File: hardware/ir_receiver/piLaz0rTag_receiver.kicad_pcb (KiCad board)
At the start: 2 copper layers, 47 x 43.2 mm, 5 parts

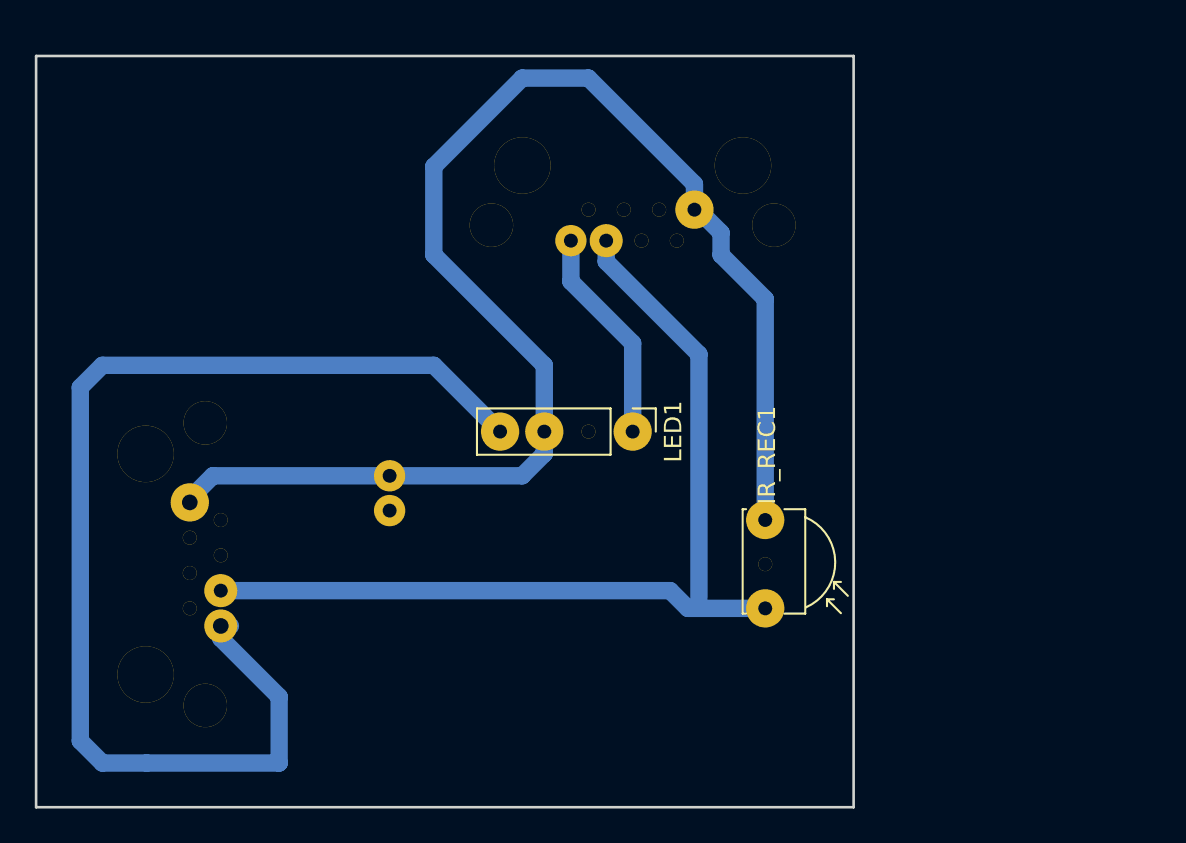
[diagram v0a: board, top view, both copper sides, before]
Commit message: Fix brocken cnc stuff
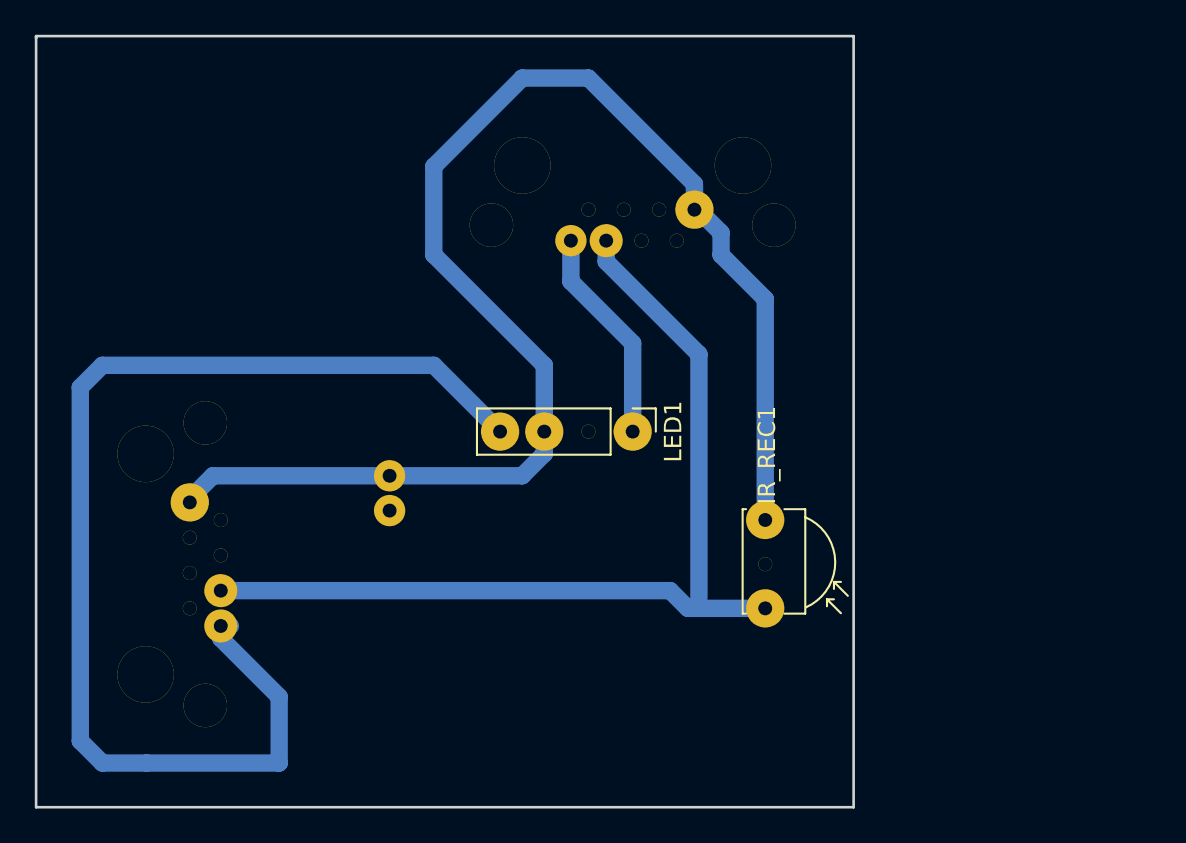
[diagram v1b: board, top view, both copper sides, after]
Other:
- board size 47 x 43.2 mm -> 47 x 44.3 mm
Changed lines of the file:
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@@
     (links 28)
     (no_connects 1)
-    (area 75.1618 110.0868 124.535001 155.650001)
+    (area 74.8618 109.7868 124.690001 155.650001)
     (thickness 1.6)
-    (drawings 10)
+    (drawings 11)
     (tracks 41)
     (zones 0)
@@
     (mod_text_size 1 1)
     (mod_text_width 0.15)
-    (pad_size 1.8 1.8)
+    (pad_size 1.9 1.9)
     (pad_drill 0.8)
     (pad_to_mask_clearance 0.2)
@@
     (pad 3 thru_hole circle (at 1.52146 -0.05588 90) (size 0.8 0.8) (drill 0.8) (layers *.Cu *.Mask)
       (net 2 GND))
-    (pad 1 thru_hole circle (at 3.55092 -0.05588 90) (size 2.2 2.2) (drill 0.9) (layers *.Cu *.Mask)
+    (pad 1 thru_hole circle (at 3.55092 -0.05588 90) (size 2.2 2.2) (drill 0.8) (layers *.Cu *.Mask)
       (net 1 +5V))
     (pad 2 thru_hole circle (at 2.53746 1.72466 90) (size 0.8 0.8) (drill 0.8) (layers *.Cu *.Mask)
@@
     (pad 7 thru_hole circle (at -2.53746 -0.05588 90) (size 0.8 0.8) (drill 0.8) (layers *.Cu *.Mask)
       (net 2 GND))
-    (pad 8 thru_hole circle (at -3.55092 1.72466 90) (size 1.9 1.9) (drill 0.9) (layers *.Cu *.Mask)
+    (pad 8 thru_hole circle (at -3.55092 1.72466 90) (size 1.9 1.9) (drill 0.8) (layers *.Cu *.Mask)
       (net 4 /LedIn))
     (pad 13 thru_hole circle (at -8.12038 0.83312 90) (size 2.49936 2.49936) (drill 2.49936) (layers *.Cu *.Mask)
@@
     )
   )
-  (gr_line (start 77.47 112.395) (end 77.47 155.575) (angle 90) (layer Edge.Cuts) (width 0.15))
-  (gr_line (start 124.46 112.395) (end 77.47 112.395) (angle 90) (layer Edge.Cuts) (width 0.15))
-  (gr_line (start 124.46 155.575) (end 124.46 112.395) (angle 90) (layer Edge.Cuts) (width 0.15))
-  (gr_line (start 77.47 155.575) (end 124.46 155.575) (angle 90) (layer Edge.Cuts) (width 0.15))
+  (gr_line (start 77.47 111.252) (end 77.47 111.379) (angle 90) (layer Edge.Cuts) (width 0.15))
+  (gr_line (start 77.47 155.575) (end 77.47 111.252) (angle 90) (layer Edge.Cuts) (width 0.15))
+  (gr_line (start 124.46 155.575) (end 77.47 155.575) (angle 90) (layer Edge.Cuts) (width 0.15))
+  (gr_line (start 124.46 111.252) (end 124.46 155.575) (angle 90) (layer Edge.Cuts) (width 0.15))
+  (gr_line (start 77.47 111.252) (end 124.46 111.252) (angle 90) (layer Edge.Cuts) (width 0.15))
   (gr_line (start 101.6 131.445) (end 101.6 141.605) (angle 90) (layer Dwgs.User) (width 0.2))
   (gr_line (start 121.92 131.445) (end 101.6 131.445) (angle 90) (layer Dwgs.User) (width 0.2))
@@
   (segment (start 115.57 120.97004) (end 115.31092 121.22912) (width 1) (layer B.Cu) (net 1) (status 30))
   (segment (start 110.23854 123.00966) (end 110.23854 124.20854) (width 1) (layer B.Cu) (net 3))
+  (segment (start 110.23854 124.20854) (end 115.57 129.54) (width 1) (layer B.Cu) (net 3))
   (segment (start 115.57 129.54) (end 115.57 143.51) (width 1) (layer B.Cu) (net 3))
-  (segment (start 110.23854 124.20854) (end 115.57 129.54) (width 1) (layer B.Cu) (net 3))
   (segment (start 88.08466 143.12646) (end 113.91646 143.12646) (width 1) (layer B.Cu) (net 3))
   (segment (start 114.935 144.145) (end 119.38 144.145) (width 1) (layer B.Cu) (net 3))
@@
     (polygon
       (pts
-        (xy 124.46 112.395) (xy 77.47 112.395) (xy 77.47 155.575) (xy 124.46 155.575)
+        (xy 124.46 111.252) (xy 77.47 111.252) (xy 77.47 155.575) (xy 124.46 155.575)
       )
     )

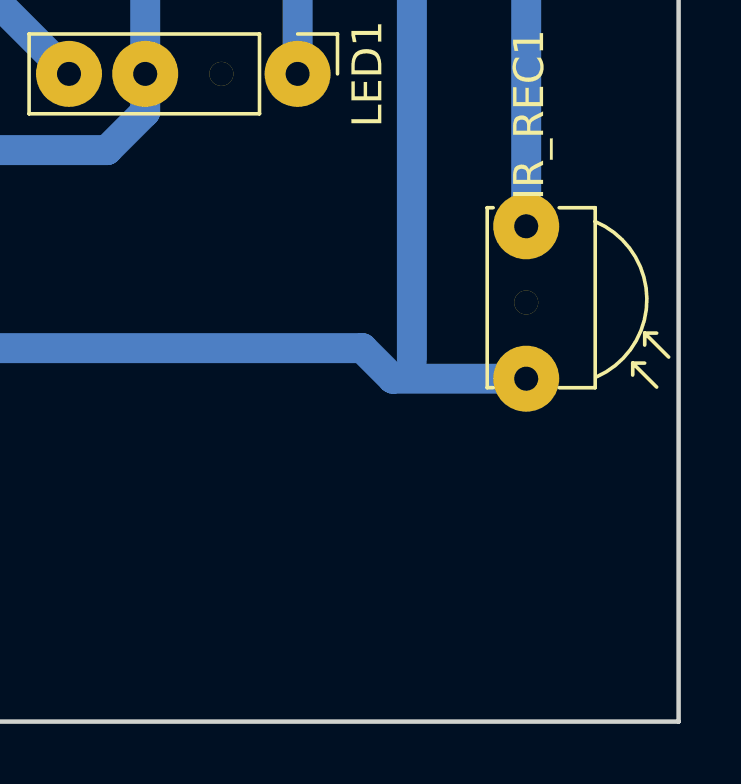
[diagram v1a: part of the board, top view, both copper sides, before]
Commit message: Add drill hole for fresnel lens
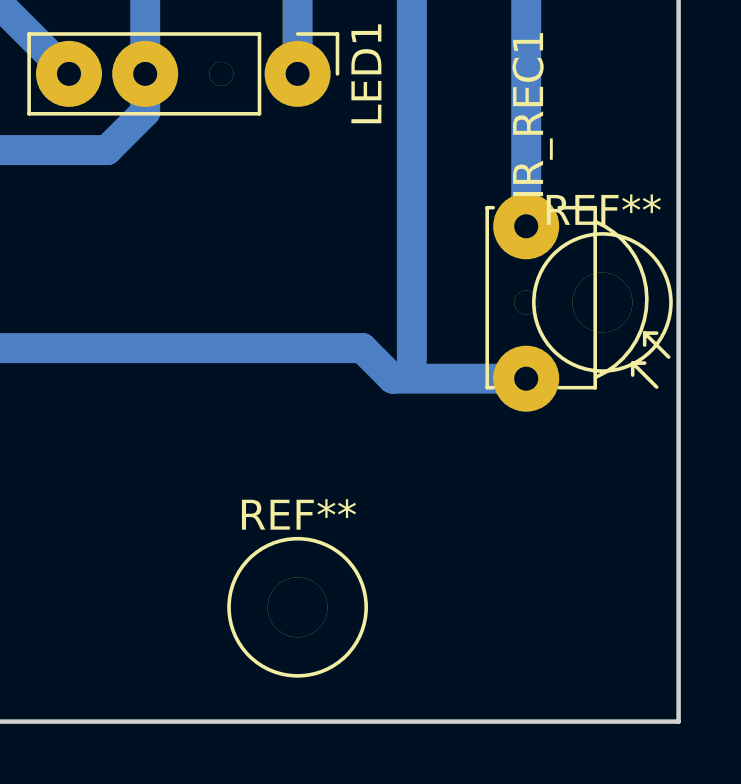
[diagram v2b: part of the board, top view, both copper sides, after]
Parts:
- added REF**: 1pin, Connectors:1pin, F.Cu at (111.8, 151.8)
- added REF**: 1pin, Connectors:1pin, F.Cu at (121.9, 141.6)
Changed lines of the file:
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@@
 (kicad_pcb (version 4) (host pcbnew 4.0.7-e2-6376~61~ubuntu18.04.1)
   (general
-    (links 28)
+    (links 30)
     (no_connects 1)
-    (area 74.8618 109.7868 124.690001 155.650001)
+    (area 74.8618 109.7868 125.045001 156.14)
     (thickness 1.6)
     (drawings 11)
     (tracks 41)
     (zones 0)
-    (modules 5)
+    (modules 7)
     (nets 6)
   )
@@
     (mod_text_size 1 1)
     (mod_text_width 0.15)
-    (pad_size 1.9 1.9)
-    (pad_drill 0.8)
+    (pad_size 2 2)
+    (pad_drill 2)
     (pad_to_mask_clearance 0.2)
     (aux_axis_origin 77.47 155.575)
@@
     )
   )
+  (module Connectors:1pin (layer F.Cu)
+    (at 111.76 151.765)
+    (descr "module 1 pin (ou trou mecanique de percage)")
+    (tags DEV)
+    (fp_text reference REF** (at 0 -3.048) (layer F.SilkS)
+      (effects (font (size 1 1) (thickness 0.15)))
+    )
+    (fp_text value 1pin (at 0 3) (layer F.Fab)
+      (effects (font (size 1 1) (thickness 0.15)))
+    )
+    (fp_circle (center 0 0) (end 2 0.8) (layer F.Fab) (width 0.1))
+    (fp_circle (center 0 0) (end 2.6 0) (layer F.CrtYd) (width 0.05))
+    (fp_circle (center 0 0) (end 0 -2.286) (layer F.SilkS) (width 0.12))
+    (pad 1 thru_hole circle (at 0 0) (size 2 2) (drill 2) (layers *.Cu *.Mask)
+      (net 2 GND))
+  )
+  (module Connectors:1pin (layer F.Cu)
+    (at 121.92 141.605)
+    (descr "module 1 pin (ou trou mecanique de percage)")
+    (tags DEV)
+    (fp_text reference REF** (at 0 -3.048) (layer F.SilkS)
+      (effects (font (size 1 1) (thickness 0.15)))
+    )
+    (fp_text value 1pin (at 0 3) (layer F.Fab)
+      (effects (font (size 1 1) (thickness 0.15)))
+    )
+    (fp_circle (center 0 0) (end 2 0.8) (layer F.Fab) (width 0.1))
+    (fp_circle (center 0 0) (end 2.6 0) (layer F.CrtYd) (width 0.05))
+    (fp_circle (center 0 0) (end 0 -2.286) (layer F.SilkS) (width 0.12))
+    (pad 1 thru_hole circle (at 0 0) (size 2 2) (drill 2) (layers *.Cu *.Mask)
+      (net 2 GND))
+  )
   (gr_line (start 77.47 111.252) (end 77.47 111.379) (angle 90) (layer Edge.Cuts) (width 0.15))

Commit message: New better receiver layout file
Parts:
- removed REF** (x2): 1pin, Connectors:1pin
- IR_REC1: moved to B.Cu
- moved ConOut1 29.2 mm to (132.6, 141.7), turned to 270 degrees
- moved IR_REC1 5.12 mm to (118.7, 139.1), turned to 270 degrees
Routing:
- net +5V: track 81.9 -> 94.1 mm
- net /LedOut: track 12.8 -> 21.7 mm
- net /IrData: track 54.4 -> 46.5 mm
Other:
- board size 47 x 44.3 mm -> 63.8 x 44.3 mm

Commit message: Some more changes for the cnc
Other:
- board size 63.8 x 44.3 mm -> 63.5 x 26.7 mm
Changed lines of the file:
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@@
     (links 28)
     (no_connects 0)
-    (area 74.8618 109.7868 125.045001 156.14)
+    (area 74.8618 128.194999 144.2386 155.015001)
     (thickness 1.6)
-    (drawings 12)
-    (tracks 43)
+    (drawings 10)
+    (tracks 44)
     (zones 0)
     (modules 5)
@@
     (last_trace_width 1)
     (trace_clearance 0.5)
-    (zone_clearance 0.6)
+    (zone_clearance 0.508)
     (zone_45_only no)
     (trace_min 0.2)
@@
     (pad_drill 2)
     (pad_to_mask_clearance 0.2)
-    (aux_axis_origin 77.47 155.575)
+    (aux_axis_origin 77.978 154.94)
     (visible_elements FFFFFF7F)
     (pcbplotparams
@@
     )
   )
-  (gr_line (start 141.224 155.575) (end 141.224 127.508) (angle 90) (layer Edge.Cuts) (width 0.15))
-  (gr_line (start 77.47 155.575) (end 141.224 155.575) (angle 90) (layer Edge.Cuts) (width 0.15))
-  (gr_line (start 77.47 127.508) (end 77.47 155.575) (angle 90) (layer Edge.Cuts) (width 0.15))
-  (gr_line (start 141.224 127.508) (end 77.47 127.508) (angle 90) (layer Edge.Cuts) (width 0.15))
-  (dimension 27.432 (width 0.3) (layer Dwgs.User)
-    (gr_text "27,432 mm" (at 157.814 142.24 270) (layer Dwgs.User)
-      (effects (font (size 1.5 1.5) (thickness 0.3)))
-    )
-    (feature1 (pts (xy 144.78 155.956) (xy 159.164 155.956)))
-    (feature2 (pts (xy 144.78 128.524) (xy 159.164 128.524)))
-    (crossbar (pts (xy 156.464 128.524) (xy 156.464 155.956)))
-    (arrow1a (pts (xy 156.464 155.956) (xy 155.877579 154.829496)))
-    (arrow1b (pts (xy 156.464 155.956) (xy 157.050421 154.829496)))
-    (arrow2a (pts (xy 156.464 128.524) (xy 155.877579 129.650504)))
-    (arrow2b (pts (xy 156.464 128.524) (xy 157.050421 129.650504)))
-  )
-  (gr_line (start 77.47 111.252) (end 77.47 111.379) (angle 90) (layer Edge.Cuts) (width 0.15))
+  (gr_line (start 77.978 128.27) (end 77.978 154.94) (angle 90) (layer Edge.Cuts) (width 0.15))
+  (gr_line (start 141.478 128.27) (end 77.978 128.27) (angle 90) (layer Edge.Cuts) (width 0.15))
+  (gr_line (start 141.478 154.94) (end 141.478 128.27) (angle 90) (layer Edge.Cuts) (width 0.15))
+  (gr_line (start 77.978 154.94) (end 141.478 154.94) (angle 90) (layer Edge.Cuts) (width 0.15))
   (gr_line (start 101.6 131.445) (end 101.6 141.605) (angle 90) (layer Dwgs.User) (width 0.2))
   (gr_line (start 121.92 131.445) (end 101.6 131.445) (angle 90) (layer Dwgs.User) (width 0.2))
@@
   (gr_line (start 101.6 141.605) (end 101.6 151.765) (angle 90) (layer Dwgs.User) (width 0.2))
   (gr_circle (center 111.76 141.665) (end 111.76 151.665) (layer Dwgs.User) (width 0.2))
-  (segment (start 106.68 133.985) (end 106.68 130.556) (width 1) (layer B.Cu) (net 1))
-  (segment (start 139.192 138.7348) (end 132.64388 145.28292) (width 1) (layer B.Cu) (net 1))
-  (segment (start 139.192 132.588) (end 139.192 138.7348) (width 1) (layer B.Cu) (net 1))
-  (segment (start 137.16 130.556) (end 139.192 132.588) (width 1) (layer B.Cu) (net 1))
-  (segment (start 135.128 130.556) (end 137.16 130.556) (width 1) (layer B.Cu) (net 1))
-  (segment (start 132.08 130.556) (end 135.128 130.556) (width 1) (layer B.Cu) (net 1))
-  (segment (start 106.68 130.556) (end 132.08 130.556) (width 1) (layer B.Cu) (net 1))
+  (segment (start 132.64388 145.28292) (end 133.86308 145.28292) (width 1) (layer B.Cu) (net 1))
+  (segment (start 106.68 131.064) (end 106.68 133.985) (width 1) (layer B.Cu) (net 1))
+  (segment (start 106.426 130.81) (end 106.68 131.064) (width 1) (layer B.Cu) (net 1))
+  (segment (start 110.998 130.81) (end 106.426 130.81) (width 1) (layer B.Cu) (net 1))
+  (segment (start 136.652 130.81) (end 110.998 130.81) (width 1) (layer B.Cu) (net 1))
+  (segment (start 138.938 133.096) (end 136.652 130.81) (width 1) (layer B.Cu) (net 1))
+  (segment (start 138.938 140.208) (end 138.938 133.096) (width 1) (layer B.Cu) (net 1))
+  (segment (start 133.86308 145.28292) (end 138.938 140.208) (width 1) (layer B.Cu) (net 1))
   (segment (start 132.64388 145.28292) (end 132.08508 145.28292) (width 1) (layer B.Cu) (net 1))
   (segment (start 132.08508 145.28292) (end 129.54 147.828) (width 1) (layer B.Cu) (net 1))
@@
   (segment (start 132.64388 145.28292) (end 132.64388 145.74012) (width 1) (layer B.Cu) (net 1))
   (segment (start 106.68 133.985) (end 106.68 135.255) (width 1) (layer B.Cu) (net 1))
+  (segment (start 105.41 136.525) (end 97.79 136.525) (width 1) (layer B.Cu) (net 1))
   (segment (start 106.68 135.255) (end 105.41 136.525) (width 1) (layer B.Cu) (net 1))
-  (segment (start 105.41 136.525) (end 97.79 136.525) (width 1) (layer B.Cu) (net 1))
   (segment (start 86.30412 138.05408) (end 86.30412 137.85088) (width 1) (layer B.Cu) (net 1))
   (segment (start 86.30412 137.85088) (end 87.63 136.525) (width 1) (layer B.Cu) (net 1))
@@
   (segment (start 130.60426 137.922) (end 130.86334 138.18108) (width 1) (layer B.Cu) (net 5) (status 30))
   (zone (net 2) (net_name GND) (layer B.Cu) (hatch edge 0.508)
-    (connect_pads yes (clearance 0.6))
-    (min_thickness 0.554)
+    (connect_pads yes (clearance 0.508))
+    (min_thickness 0.254)
     (fill yes (arc_segments 16) (thermal_gap 0.508) (thermal_bridge_width 0.508))
     (polygon
       (pts
-        (xy 141.224 127.508) (xy 77.47 127.508) (xy 77.47 155.575) (xy 141.224 155.575)
+        (xy 77.978 128.27) (xy 141.478 128.27) (xy 141.478 154.94) (xy 77.978 154.94)
       )
     )
